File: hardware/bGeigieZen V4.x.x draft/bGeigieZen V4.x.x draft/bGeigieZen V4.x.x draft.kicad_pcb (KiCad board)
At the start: 2 copper layers, 129.4 x 64.6 mm, 12 parts, among them J1 M5 2x15 pin, J2 Geiger IRover, J3 GPS, J4 Geiger Safepulse, J5 Extra support header, J6 Grove

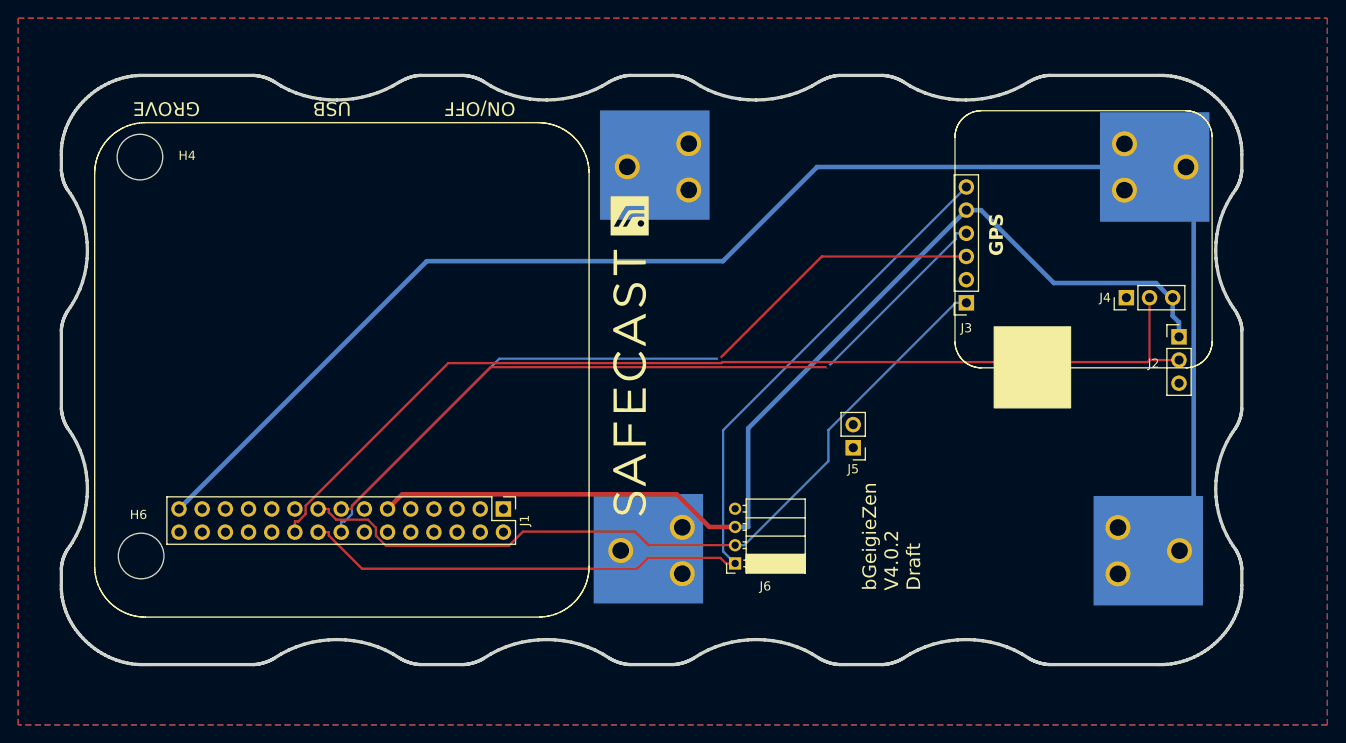
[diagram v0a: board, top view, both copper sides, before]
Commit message: Tested black color boards for production.
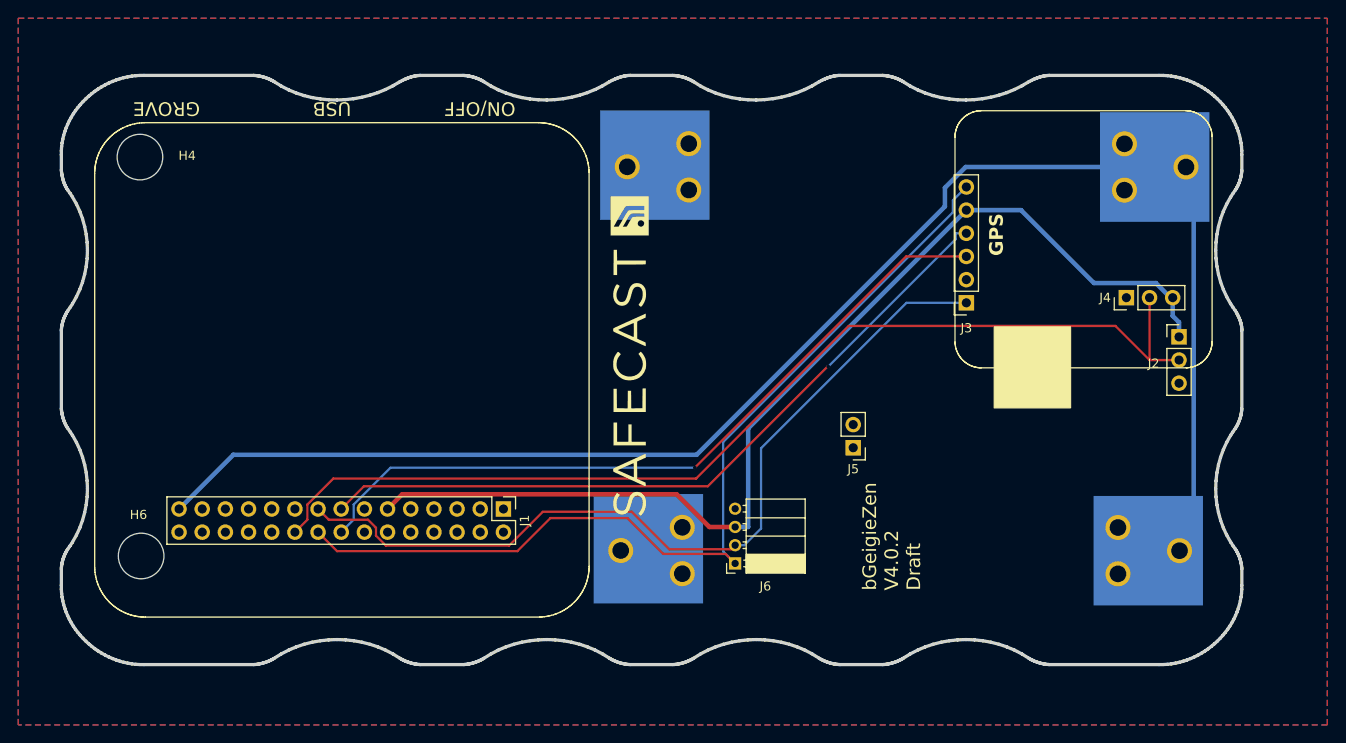
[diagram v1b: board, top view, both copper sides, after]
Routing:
- net /SDA: track 87.7 -> 92.8 mm
- net /GIO2 on Core and GIO32 on Core-2: track 112.8 -> 115.6 mm
- net /SCL: track 101.2 -> 103.0 mm
- net /BAT: track 172.4 -> 173.6 mm

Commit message: Updated versions to reflect the board numbering as we agreed in last meeting
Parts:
- moved BT2 1.42 mm to (177.0, 120.1)
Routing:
- net /BAT: track 173.6 -> 174.8 mm
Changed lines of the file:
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@@
 	(footprint "Library:BATTERY_18650-HOLDER"
 		(layer "B.Cu")
-		(at 176.5344 118.7592 180)
+		(at 177.0424 120.08 180)
 		(descr "<h3>18650 Lithium Ion Cell Battery Holders</h3><p>PCB mount clips properly spaced to hold a 18650 Lithium Ion Cell battery.</p><p><a href=\"https://cdn.sparkfun.com/datasheets/Prototyping/54.PDF\">Datasheet</a></p><h4>Devices Using</h4><ul><li>BATTERY</li></ul>")
 		(property "Reference" "BT2"
@@
 	)
 	(segment
+		(start 207.1624 118.7692)
+		(end 210.1088 115.8228)
+		(width 0.5)
+		(layer "B.Cu")
+		(net 27)
+	)
+	(segment
 		(start 181.4437 81.0387)
 		(end 154.2288 108.2536)
@@
 	)
 	(segment
-		(start 207.1624 118.7692)
-		(end 208.7179 117.2137)
-		(width 0.5)
-		(layer "B.Cu")
-		(net 27)
-	)
-	(segment
 		(start 204.4456 76.7068)
 		(end 183.720658 76.7068)
@@
 	)
 	(segment
-		(start 208.7179 117.2137)
-		(end 208.7179 77.5511)
-		(width 0.5)
-		(layer "B.Cu")
-		(net 27)
-	)
-	(segment
 		(start 154.2288 108.2536)
 		(end 103.4288 108.2536)
@@
 	)
 	(segment
-		(start 208.7179 77.5511)
-		(end 207.8736 76.7068)
+		(start 183.720658 76.7068)
+		(end 181.4437 78.983758)
 		(width 0.5)
 		(layer "B.Cu")
@@
 	)
 	(segment
-		(start 183.720658 76.7068)
-		(end 181.4437 78.983758)
+		(start 210.1088 115.8228)
+		(end 210.1088 78.942)
 		(width 0.5)
 		(layer "B.Cu")
@@
 		(width 0.5)
 		(layer "B.Cu")
+		(net 27)
+	)
+	(segment
+		(start 210.1088 78.942)
+		(end 207.8736 76.7068)
+		(width 0.5)
+		(layer "B.Cu")

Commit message: V4.0.3 boards
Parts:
- added G***: LOGO, bGeigieRaku_M5_1015:18650 map, B.Cu at (177.7, 119.9)
- added G***: LOGO, bGeigieRaku_M5_1015:18650 map, B.Cu at (178.0, 76.4)
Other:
- board text added: "bGeigieZen V4.0.3 Draft"
- board text removed: "bGeigieZen V4.0.2 Draft"
